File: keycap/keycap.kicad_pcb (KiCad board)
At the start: 2 copper layers, 15.5 x 15.5 mm, 14 parts, among them J1 Conn_01x01_Female, J10 Conn_01x01_Female, J2 Conn_01x01_Female, J3 Conn_01x01_Female, J4 Conn_01x01_Female, J5 Conn_01x01_Female, J6 Conn_01x01_Female, J7 Conn_01x01_Female, J8 Conn_01x01_Female, J9 Conn_01x01_Female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

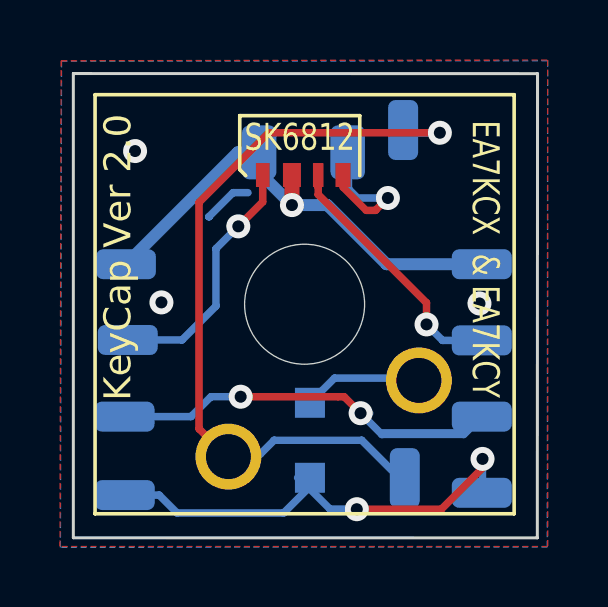
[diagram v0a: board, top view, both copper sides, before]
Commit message: Update design to use the SK6812-E
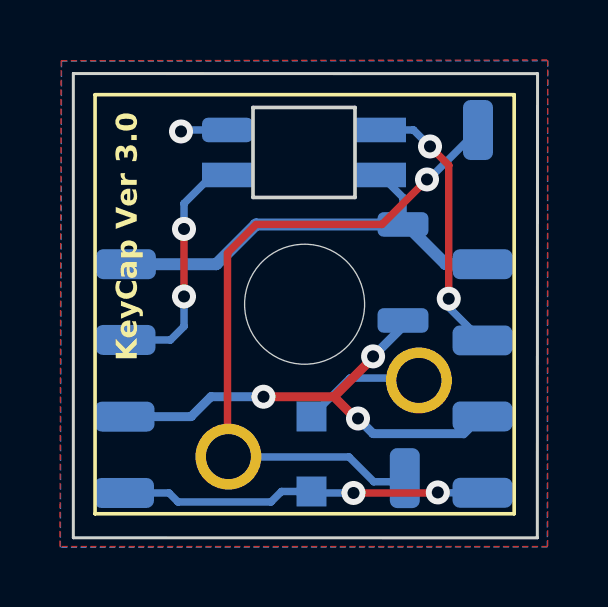
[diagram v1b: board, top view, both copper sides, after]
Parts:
- removed C1: 0.1uF, Capacitor_SMD:C_1206_3216Metric
- removed REF**: SK6812, Battery:LED_SK6812_4020_
- added ?: , , F.Cu at (124.4, 110.6)
- added ?: , , F.Cu at (124.4, 113.8)
- added SK6812-E: SK6812-MINI-E, Keebio-Parts:SK6812-MINI-E, B.Cu at (121.1, 108.2)
- moved J9 2.50 mm to (126.9, 107.5)
- moved D1 0.46 mm to (121.3, 118.2)
- moved J10 0.08 mm to (115.1, 119.5)
- moved J2 0.07 mm to (115.2, 114.4)
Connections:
- net Net-(D1-Pad2) renamed COL2ROW
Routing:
- net /ROW: track 15.9 -> 11.9 mm
- net /VCC: track 18.0 -> 14.8 mm, vias 1 -> 0
- net /COL: track 25.9 -> 23.2 mm
- net (no net): track 1.65 -> 0.00 mm
- net GND: track 18.8 -> 18.1 mm, vias 6 -> 4
- net /DIN: track 8.52 -> 8.11 mm, vias 1 -> 2
- net /DOUT: track 8.95 -> 9.34 mm, vias 1 -> 2
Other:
- net class Default removed
- board text added: "KeyCap Ver 3.0"
- board text removed: "EA7KCX & EA7KCY"
- board text removed: "KeyCap Ver 2.0"
